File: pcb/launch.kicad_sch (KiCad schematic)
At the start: 249 parts, among them J1 Conn_ARM_SWD_TagConnect_TC2030, J7 AFC07-S20FCC-00, SW1 SKRPACE010, SW2 SKRPACE010, U1 RP2040, U24 W25Q16JVSSIQ, Y2 RH100-12.000-18-2030-TR

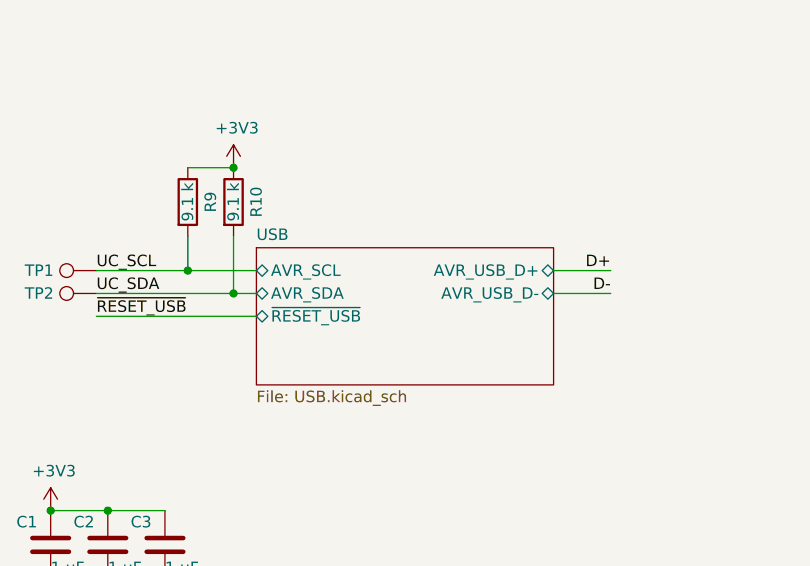
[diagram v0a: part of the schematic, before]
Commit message: change AVR to UC on some net names since we don't have an Atmel AVR controller now
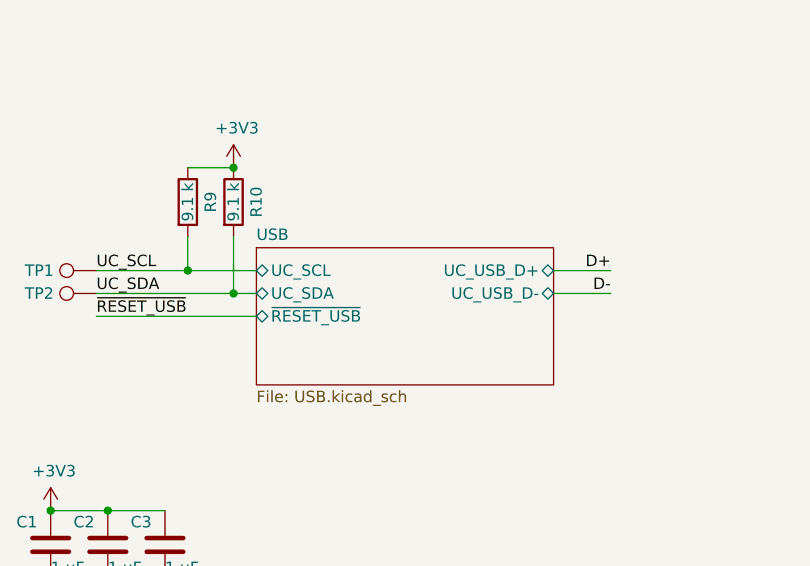
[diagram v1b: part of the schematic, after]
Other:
- sheet USB ports: added UC_SCL, UC_SDA, UC_USB_D+, UC_USB_D-; removed AVR_SCL, AVR_SDA, AVR_USB_D+, AVR_USB_D-
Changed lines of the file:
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@@
   (title_block
     (title "Launch")
-    (date "2023-01-31")
+    (date "2023-02-03")
     (rev "pre 3.0")
     (company "System76")
@@
       (effects (font (size 1.27 1.27)) (justify left top))
     )
-    (pin "AVR_USB_D+" bidirectional (at 374.65 39.37 0)
+    (pin "UC_USB_D+" bidirectional (at 374.65 39.37 0)
       (effects (font (size 1.27 1.27)) (justify right))
     )
-    (pin "AVR_USB_D-" bidirectional (at 374.65 41.91 0)
+    (pin "UC_USB_D-" bidirectional (at 374.65 41.91 0)
       (effects (font (size 1.27 1.27)) (justify right))
     )
-    (pin "AVR_SCL" bidirectional (at 341.63 39.37 180)
+    (pin "UC_SCL" bidirectional (at 341.63 39.37 180)
       (effects (font (size 1.27 1.27)) (justify left))
     )
-    (pin "AVR_SDA" bidirectional (at 341.63 41.91 180)
+    (pin "UC_SDA" bidirectional (at 341.63 41.91 180)
       (effects (font (size 1.27 1.27)) (justify left))
     )

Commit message: add 2nd SWD connector, BOM edits, export
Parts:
- added J6: SWD_TH, Connector_PinHeader_2.54mm:PinHeader_1x04_P2.54mm_Vertical, symbol Connector_Generic:Conn_01x04
- C70, C71: Manufacturer (none) -> Generic NP0 capacitor
- C72, C73: Manufacturer (none) -> Generic X5R capacitor
- R35, R36, R37, R38, R39: Manufacturer (none) -> Generic 1% resistor
- U1: Manufacturer (none) -> Raspberry Pi
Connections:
- net +3V3: now also J6.1 (Pin_1)
- net GND: now also J6.4 (Pin_4)
- net SWCLK: now also J6.3 (Pin_3)
- net SWDIO: now also J6.2 (Pin_2)
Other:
- note added: "Alternate SWD connector"
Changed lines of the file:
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@@
     (title "Launch")
     (date "2023-02-03")
-    (rev "pre 3.0")
+    (rev "3.0")
     (company "System76")
   )
@@
     (stroke (width 0) (type default))
   )
+  (wire (pts (xy 341.63 213.36) (xy 349.25 213.36))
+    (stroke (width 0) (type default))
+  )
   (wire (pts (xy 62.23 76.2) (xy 62.23 88.9))
     (stroke (width 0) (type default))
@@
     (stroke (width 0) (type default))
   )
+  (wire (pts (xy 341.63 210.82) (xy 349.25 210.82))
+    (stroke (width 0) (type default))
+  )
   (wire (pts (xy 17.78 241.3) (xy 17.78 227.33))
     (stroke (width 0) (type default))
@@
     (stroke (width 0) (type default))
   )
+  (text "Alternate SWD\nconnector" (at 332.74 205.74 0)
+    (effects (font (size 1.27 1.27)) (justify left bottom))
+  )
   (text "DFU:\nhold while\nreleasing\nreset for\nUSB DFU" (at 297.18 105.41 0)
     (effects (font (size 1.27 1.27)) (justify left bottom))
@@
   )
   (text "~{RESET_USB} should be\ndriven high 10 ms after\npower on. This ensures\nthe USB7206 supplies are\nup."
-    (at 367.03 217.17 0)
+    (at 381 208.28 0)
     (effects (font (size 1.27 1.27)) (justify left bottom))
   )
@@
     (effects (font (size 1.27 1.27)) (justify left bottom))
   )
-  (text "Reset" (at 287.02 101.6 0)
+  (text "Reset" (at 334.01 102.87 90)
     (effects (font (size 1.27 1.27)) (justify left bottom))
   )
@@
     (effects (font (size 1.27 1.27)) (justify left bottom))
   )
+  (label "SWCLK" (at 349.25 213.36 180) (fields_autoplaced)
+    (effects (font (size 1.27 1.27)) (justify right bottom))
+  )
   (label "XOUT1" (at 318.77 166.37 0) (fields_autoplaced)
     (effects (font (size 1.27 1.27)) (justify left bottom))
@@
     (effects (font (size 1.27 1.27)) (justify right bottom))
   )
+  (label "SWDIO" (at 349.25 210.82 180) (fields_autoplaced)
+    (effects (font (size 1.27 1.27)) (justify right bottom))
+  )
   (label "~{RESET_USB}" (at 405.13 163.83 180) (fields_autoplaced)
     (effects (font (size 1.27 1.27)) (justify right bottom))
@@
       (effects (font (size 1.27 1.27)) hide)
     )
+    (property "Manufacturer" "Generic X5R capacitor" (at 350.52 93.98 0)
+      (effects (font (size 1.27 1.27)) hide)
+    )
     (pin "1")
     (pin "2")
@@
       (effects (font (size 1.27 1.27)) hide)
     )
+    (property "Manufacturer" "Generic NP0 capacitor" (at 285.75 166.37 0)
+      (effects (font (size 1.27 1.27)) hide)
+    )
     (pin "1")
     (pin "2")
@@
       (effects (font (size 1.27 1.27)) hide)
     )
+    (property "Manufacturer" "Generic 1% resistor" (at 323.85 144.78 0)
+      (effects (font (size 1.27 1.27)) hide)
+    )
     (pin "1")
     (pin "2")
@@
       (effects (font (size 1.27 1.27)) hide)
     )
+    (property "Manufacturer" "Generic 1% resistor" (at 331.47 88.9 0)
+      (effects (font (size 1.27 1.27)) hide)
+    )
     (pin "1")
     (pin "2")
@@
       (effects (font (size 1.27 1.27)) hide)
     )
+    (property "Manufacturer" "Generic NP0 capacitor" (at 285.75 158.75 0)
+      (effects (font (size 1.27 1.27)) hide)
+    )
     (pin "1")
     (pin "2")
@@
     )
   )
+  (symbol (lib_id "power:GND") (at 341.63 215.9 0) (unit 1)
+    (in_bom yes) (on_board yes) (dnp no)
+    (property "Reference" "#PWR0214" (at 341.63 222.25 0)
+      (effects (font (size 1.27 1.27)) hide)
+    )
+    (property "Value" "GND" (at 341.757 220.2942 0)
+      (effects (font (size 1.27 1.27)))
+    )
+    (property "Footprint" "" (at 341.63 215.9 0)
+      (effects (font (size 1.27 1.27)) hide)
+    )
+    (property "Datasheet" "" (at 341.63 215.9 0)
+      (effects (font (size 1.27 1.27)) hide)
+    )
+    (pin "1")
+    (instances
+      (project "launch"
+        (path "/80c969df-cd39-4c4a-8336-5a366308cfd3"
+          (reference "#PWR0214") (unit 1)
+        )
+      )
+    )
+  )
   (symbol (lib_id "QSPI_flash:W25Q16JVSSIQ") (at 311.15 125.73 0) (mirror y) (unit 1)
     (in_bom yes) (on_board yes) (dnp no)
@@
     )
   )
+  (symbol (lib_id "Connector_Generic:Conn_01x04") (at 336.55 210.82 0) (mirror y) (unit 1)
+    (in_bom no) (on_board yes) (dnp yes)
+    (property "Reference" "J6" (at 334.01 211.455 0)
+      (effects (font (size 1.27 1.27)) (justify left))
+    )
+    (property "Value" "SWD_TH" (at 334.01 213.995 0)
+      (effects (font (size 1.27 1.27)) (justify left))
+    )
+    (property "Footprint" "Connector_PinHeader_2.54mm:PinHeader_1x04_P2.54mm_Vertical" (at 336.55 210.82 0)
+      (effects (font (size 1.27 1.27)) hide)
+    )
+    (property "Datasheet" "~" (at 336.55 210.82 0)
+      (effects (font (size 1.27 1.27)) hide)
+    )
+    (pin "1")
+    (pin "2")
+    (pin "3")
+    (pin "4")
+    (instances
+      (project "launch"
+        (path "/80c969df-cd39-4c4a-8336-5a366308cfd3"
+          (reference "J6") (unit 1)
+        )
+      )
+    )
+  )
   (symbol (lib_id "Connector:Conn_ARM_SWD_TagConnect_TC2030") (at 295.91 189.23 0) (unit 1)
     (in_bom no) (on_board yes) (dnp no) (fields_autoplaced)
@@
     )
   )
+  (symbol (lib_id "power:+3V3") (at 341.63 208.28 270) (unit 1)
+    (in_bom yes) (on_board yes) (dnp no)
+    (property "Reference" "#PWR0197" (at 337.82 208.28 0)
+      (effects (font (size 1.27 1.27)) hide)
+    )
+    (property "Value" "+3V3" (at 347.98 208.28 90)
+      (effects (font (size 1.27 1.27)))
+    )
+    (property "Footprint" "" (at 341.63 208.28 0)
+      (effects (font (size 1.27 1.27)) hide)
+    )
+    (property "Datasheet" "" (at 341.63 208.28 0)
+      (effects (font (size 1.27 1.27)) hide)
+    )
+    (pin "1")
+    (instances
+      (project "launch"
+        (path "/80c969df-cd39-4c4a-8336-5a366308cfd3"
+          (reference "#PWR0197") (unit 1)
+        )
+      )
+    )
+  )
   (symbol (lib_id "power:+3V3") (at 306.07 114.3 0) (unit 1)
     (in_bom yes) (on_board yes) (dnp no) (fields_autoplaced)
@@
       (effects (font (size 1.27 1.27)) hide)
     )
+    (property "Manufacturer" "Generic 1% resistor" (at 317.5 88.9 0)
+      (effects (font (size 1.27 1.27)) hide)
+    )
     (pin "1")
     (pin "2")
@@
       (effects (font (size 1.27 1.27)) hide)
     )
+    (property "Manufacturer" "Generic 1% resistor" (at 323.85 147.32 0)
+      (effects (font (size 1.27 1.27)) hide)
+    )
     (pin "1")
     (pin "2")
@@
       (effects (font (size 1.27 1.27)) hide)
     )
+    (property "Manufacturer" "Generic X5R capacitor" (at 361.95 93.98 0)
+      (effects (font (size 1.27 1.27)) hide)
+    )
     (pin "1")
     (pin "2")
@@
       (effects (font (size 1.27 1.27)) hide)
     )
+    (property "Manufacturer" "Generic 1% resistor" (at 314.96 166.37 0)
+      (effects (font (size 1.27 1.27)) hide)
+    )
     (pin "1")
     (pin "2")
@@
       (effects (font (size 1.27 1.27)) hide)
     )
+    (property "Manufacturer" "Raspberry Pi" (at 360.68 151.13 0)
+      (effects (font (size 1.27 1.27)) hide)
+    )
